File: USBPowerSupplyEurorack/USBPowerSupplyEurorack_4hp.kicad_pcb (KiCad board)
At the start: 2 copper layers, 9.8 x 110 mm, 21 parts, among them J1 1734366-1, J2 95278-501A10LF, Q1 Q_PMOS_GSD

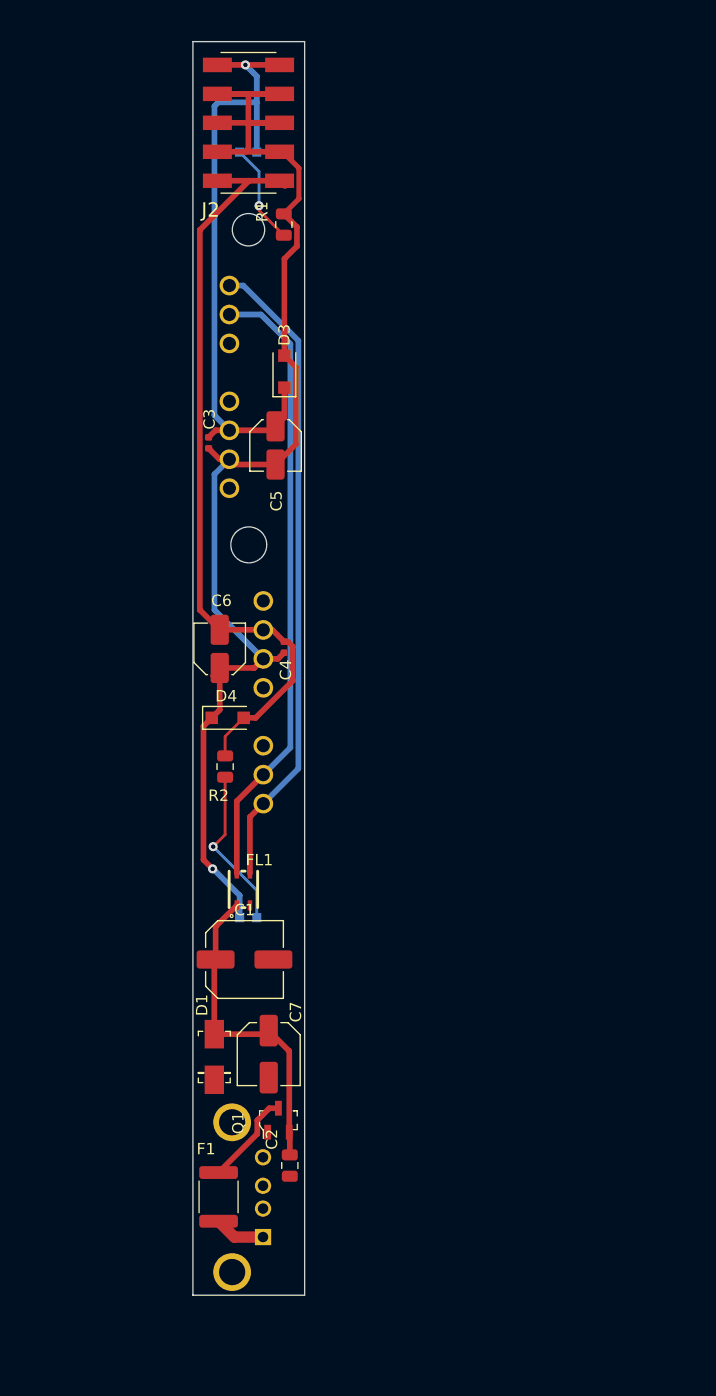
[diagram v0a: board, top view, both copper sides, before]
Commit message: going to 4hp for better routing
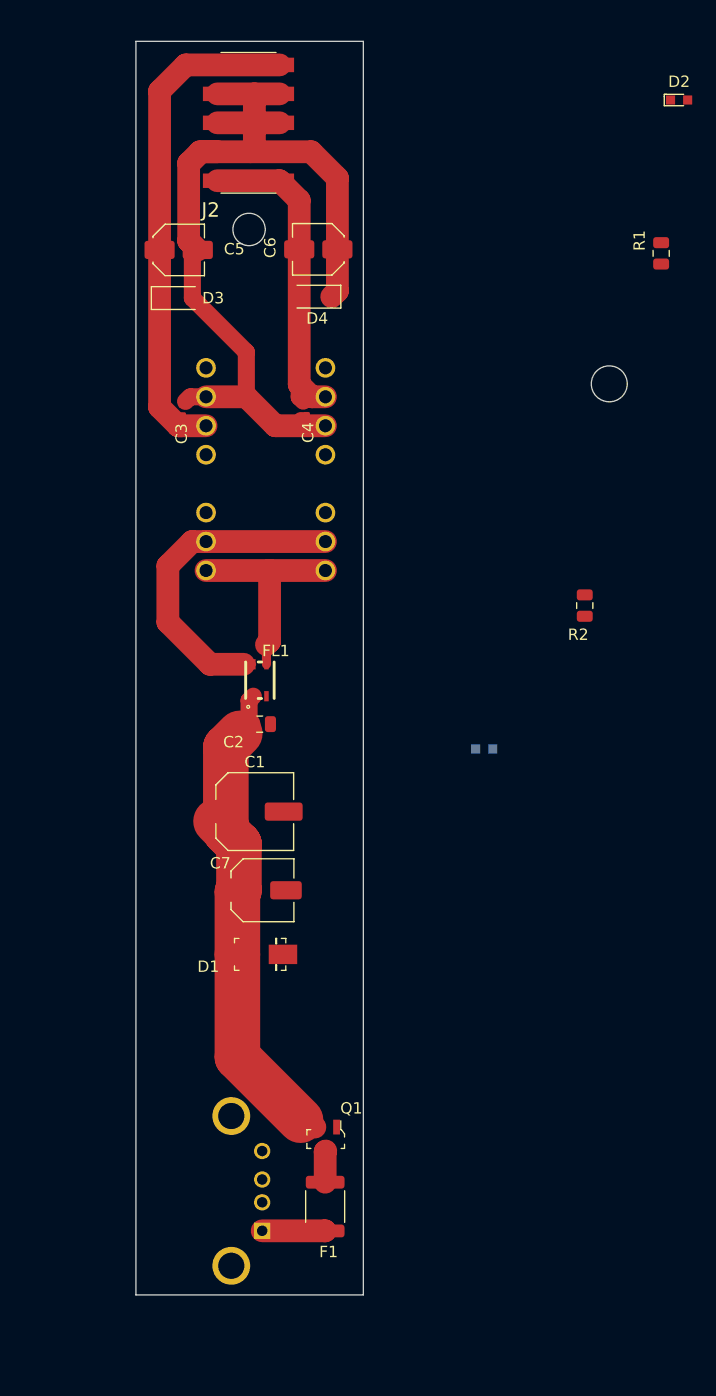
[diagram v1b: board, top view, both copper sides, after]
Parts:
- D2: moved to F.Cu
- F1: value 1812L110 -> 1.1A
- moved C2 38.8 mm to (140.4, 108.0), turned to 0 degrees
- moved D2 38.1 mm to (177.2, 53.2)
- moved D4 37.7 mm to (145.3, 70.5), turned to 180 degrees
- moved C6 36.1 mm to (145.6, 66.3), turned to 180 degrees
- moved R2 34.6 mm to (168.9, 97.6)
- moved R1 33.2 mm to (175.6, 66.7)
- moved D5 25.4 mm to (160.1, 110.2)
- moved PS1 25.1 mm to (135.7, 94.5), turned to 90 degrees
- moved PS2 21.2 mm to (146.2, 94.5)
- moved C4 20.9 mm to (144.5, 80.4)
- moved C5 19.1 mm to (133.3, 66.4), turned to 0 degrees
- moved FL1 18.4 mm to (140.4, 104.2)
- moved C7 14.4 mm to (140.7, 122.6), turned to 0 degrees
- moved C1 13.0 mm to (140.0, 115.7)
- moved D3 11.5 mm to (133.1, 70.6), turned to 0 degrees
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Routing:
- net Net-(C1-Pad1): track 28.7 -> 82.5 mm
- net -12V: track 67.7 -> 28.4 mm
- net +Vin: track 54.8 -> 28.7 mm
- net -Vin: track 56.6 -> 35.6 mm
- net Net-(D5-Pad1): track 14.3 -> 0.00 mm, vias 1 -> 0
- net 0V: track 118.4 -> 106.6 mm, vias 1 -> 0
- net Net-(D2-Pad1): track 8.89 -> 0.00 mm, vias 1 -> 0
- net +5V: track 8.28 -> 2.76 mm
- net Net-(F1-Pad1): track 4.47 -> 5.53 mm
- net +12V: track 56.4 -> 55.7 mm, vias 1 -> 0
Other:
- board size 9.8 x 110 mm -> 43.1 x 110 mm

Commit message: naive placement and routing
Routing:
- net Net-(C1-Pad1): track 82.5 -> 72.7 mm
- net +5V: track 2.76 -> 0.00 mm
- net 0V: track 106.6 -> 107.0 mm, vias 0 -> 9
- added copper zone on F.Cu, net +5V
- added copper zone on F.Cu, net -Vin
- added copper zone on B.Cu, net 0V
- added copper zone on F.Cu, net 0V
- added copper zone on F.Cu, net Net-(C1-Pad1)
- added copper zone on F.Cu, net Net-(F1-Pad1)

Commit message: changed caps on schematics, added PI filter and bigger caps as we have now 4HP
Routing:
- removed copper zone on F.Cu, net +5V
- removed copper zone on F.Cu, net -Vin
- removed copper zone on B.Cu, net 0V
- removed copper zone on F.Cu, net 0V
- removed copper zone on F.Cu, net Net-(C1-Pad1)
- removed copper zone on F.Cu, net Net-(F1-Pad1)
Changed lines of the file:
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@@
   (segment (start 135.7 94.525) (end 141.275 94.525) (width 2) (layer F.Cu) (net 10))
   (segment (start 141.275 94.525) (end 146.175 94.525) (width 2) (layer F.Cu) (net 10))
-  (zone (net 6) (net_name "Net-(F1-Pad1)") (layer F.Cu) (hatch edge 0.508)
-    (connect_pads thru_hole_only (clearance 0.108))
-    (min_thickness 0.254)
-    (fill yes (arc_segments 32) (thermal_gap 0.508) (thermal_bridge_width 0.508) (smoothing fillet) (radius 0.3))
-    (polygon
-      (pts
-        (xy 148.425 154.375) (xy 138.725 154.4) (xy 138.725 150.925) (xy 148.45 150.925)
-      )
-    )
-  )
-  (zone (net 2) (net_name +5V) (layer F.Cu) (hatch edge 0.508)
-    (connect_pads yes (clearance 0.508))
-    (min_thickness 0.254)
-    (fill yes (arc_segments 32) (thermal_gap 0.508) (thermal_bridge_width 0.508) (smoothing fillet) (radius 0.3))
-    (polygon
-      (pts
-        (xy 148.25 145.2) (xy 148.25 149.3) (xy 144.375 149.3) (xy 144.45 146.175) (xy 144.725 145.25)
-        (xy 145.95 144.75) (xy 147.45 144.725)
-      )
-    )
-  )
-  (zone (net 1) (net_name "Net-(C1-Pad1)") (layer F.Cu) (hatch edge 0.508)
-    (connect_pads thru_hole_only (clearance 0.108))
-    (min_thickness 0.254)
-    (fill yes (arc_segments 32) (thermal_gap 0.508) (thermal_bridge_width 0.508) (smoothing fillet) (radius 0.5))
-    (polygon
-      (pts
-        (xy 140.55 105.225) (xy 140.65 108.7) (xy 140.675 108.65) (xy 140.5 109.7) (xy 139.575 111.075)
-        (xy 139.575 116.275) (xy 140.575 117.425) (xy 140.575 121.25) (xy 140.625 136.45) (xy 146.2 141.725)
-        (xy 146.275 142.425) (xy 146.1 143.975) (xy 144.7 144.65) (xy 143.025 144.65) (xy 136.3 137.85)
-        (xy 136.3 121) (xy 134.55 117.1) (xy 134.55 108.725) (xy 136.725 104.775) (xy 140.55 104.775)
-      )
-    )
-  )
-  (zone (net 10) (net_name -Vin) (layer F.Cu) (hatch edge 0.508)
-    (connect_pads thru_hole_only (clearance 0.108))
-    (min_thickness 0.254)
-    (fill yes (arc_segments 32) (thermal_gap 0.508) (thermal_bridge_width 0.508) (smoothing fillet) (radius 0.5))
-    (polygon
-      (pts
-        (xy 146.25 93.65) (xy 146.625 93.675) (xy 146.975 93.95) (xy 147.2 94.3) (xy 147.125 103.225)
-        (xy 141.2 103.225) (xy 140.8 103.25) (xy 140.7 103.025) (xy 140.325 102.0125) (xy 139.725 101.2875)
-        (xy 134.975 95.425) (xy 134.7 94.625) (xy 134.925 93.975) (xy 135.45 93.625)
-      )
-    )
-  )
-  (zone (net 3) (net_name 0V) (layer F.Cu) (hatch edge 0.508)
-    (connect_pads thru_hole_only (clearance 0.254))
-    (min_thickness 0.254)
-    (fill yes (arc_segments 32) (thermal_gap 0.508) (thermal_bridge_width 0.508) (smoothing fillet) (radius 0.5))
-    (polygon
-      (pts
-        (xy 153.35 47.45) (xy 153.725 86.975) (xy 122.125 87.075) (xy 124.125 46.875)
-      )
-    )
-  )
-  (zone (net 3) (net_name 0V) (layer B.Cu) (hatch edge 0.508)
-    (connect_pads thru_hole_only (clearance 0.254))
-    (min_thickness 0.254)
-    (fill yes (arc_segments 32) (thermal_gap 0.508) (thermal_bridge_width 0.508) (smoothing fillet) (radius 0.5))
-    (polygon
-      (pts
-        (xy 154.9 87.15) (xy 121.825 86.925) (xy 119.625 46.475) (xy 157.65 46.475)
-      )
-    )
-  )
 )

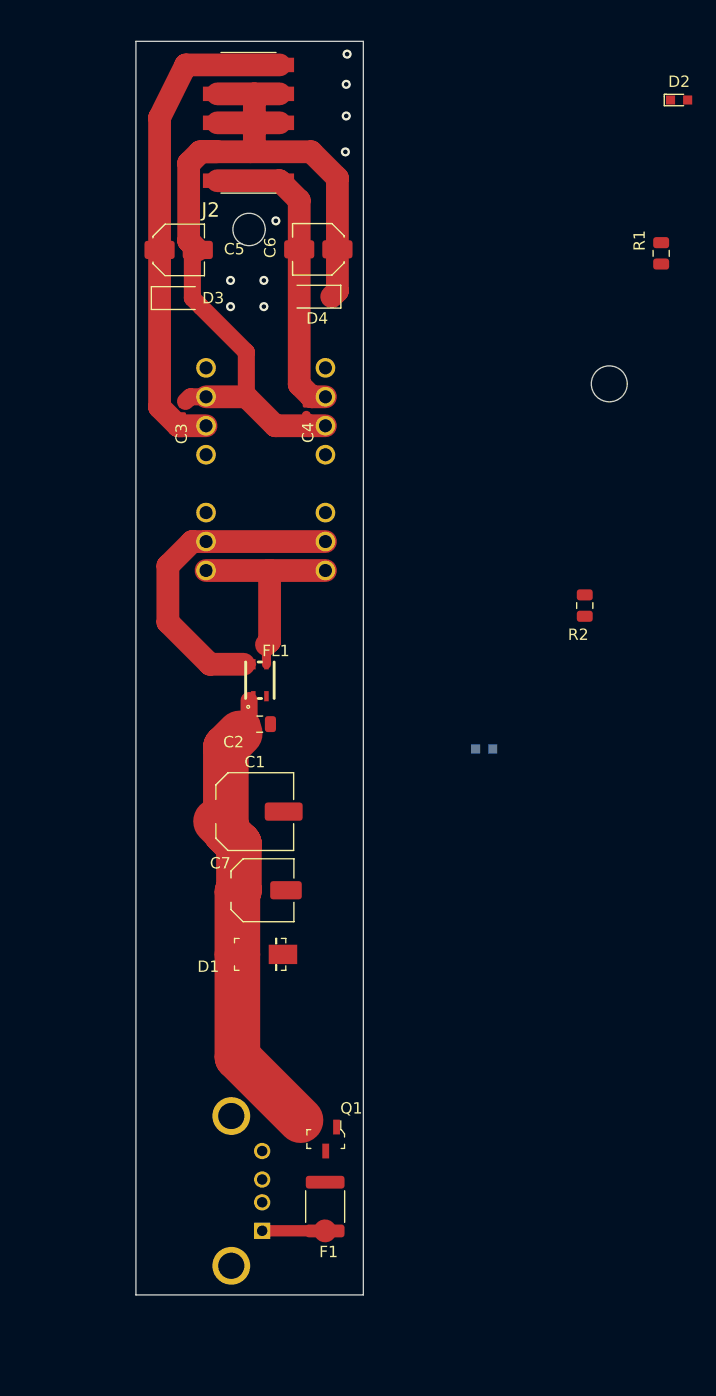
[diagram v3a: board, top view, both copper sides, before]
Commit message: new components placement
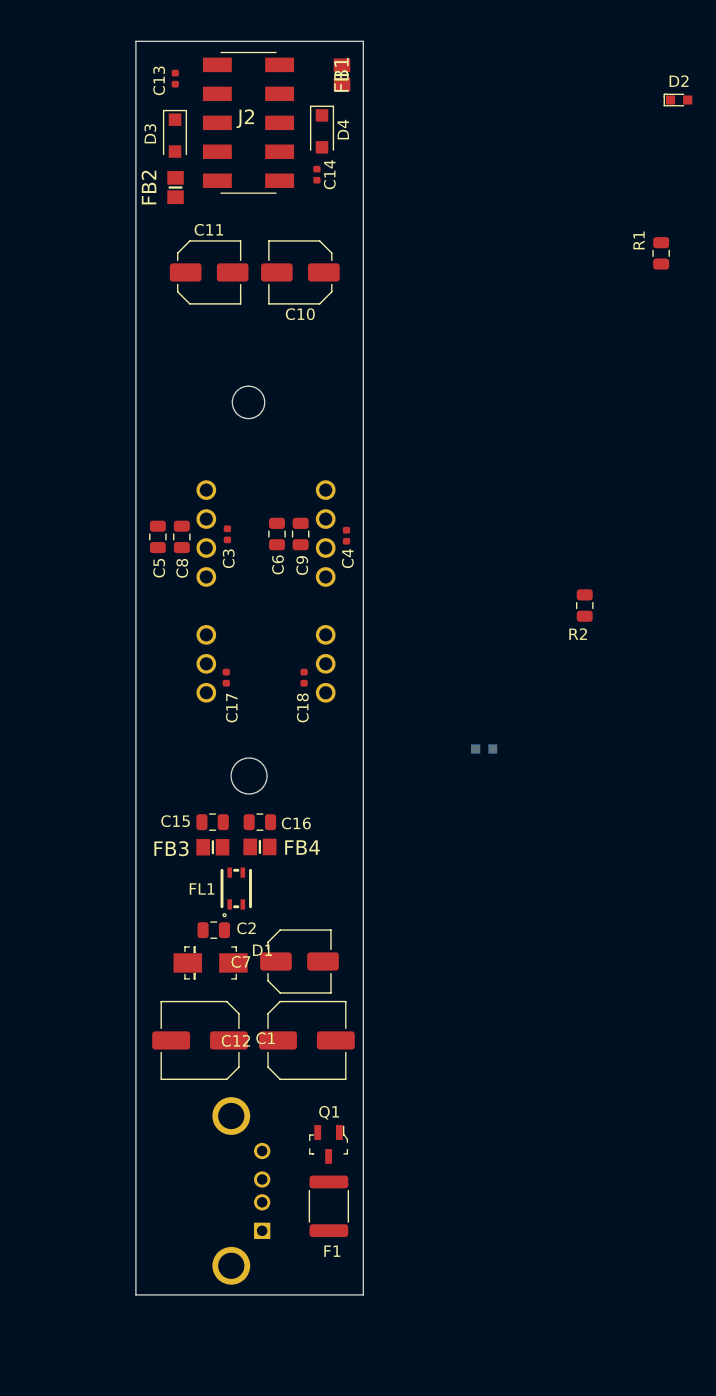
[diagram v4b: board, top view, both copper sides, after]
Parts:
- added C10: 47uF, Capacitor_SMD:C_Elec_5x5.4, F.Cu at (144.0, 68.4)
- added C11: 47uF, Capacitor_SMD:C_Elec_5x5.4, F.Cu at (136.0, 68.4)
- added C12: 220uF, Capacitor_SMD:C_Elec_6.3x7.7, F.Cu at (144.6, 135.8)
- added C13: 100nF, Capacitor_SMD:C_0402_1005Metric, F.Cu at (133.0, 51.4)
- added C14: 100nF, Capacitor_SMD:C_0402_1005Metric, F.Cu at (145.4, 59.8)
- added C15: 22uF, Capacitor_SMD:C_0805_2012Metric, F.Cu at (136.3, 116.6)
- added C16: 22uF, Capacitor_SMD:C_0805_2012Metric, F.Cu at (140.4, 116.6)
- added C17: 100nF, Capacitor_SMD:C_0402_1005Metric, F.Cu at (137.5, 103.9)
- added C18: 100nF, Capacitor_SMD:C_0402_1005Metric, F.Cu at (144.3, 103.9)
- added C8: 22uF, Capacitor_SMD:C_0805_2012Metric, F.Cu at (133.6, 91.6)
- added C9: 22uF, Capacitor_SMD:C_0805_2012Metric, F.Cu at (144.0, 91.3)
- added FB1: C15957, MPZ2012S101AT000:BEADC2012X105N, F.Cu at (147.6, 51.0)
- added FB2: C15957, MPZ2012S101AT000:BEADC2012X105N, F.Cu at (133.0, 60.9)
- added FB3: C15957, MPZ2012S101AT000:BEADC2012X105N, F.Cu at (136.3, 118.8)
- added FB4: C15957, MPZ2012S101AT000:BEADC2012X105N, F.Cu at (140.4, 118.8)
- C5, C6: value 4.7uF -> 22uF; footprint Capacitor_SMD:C_Elec_4x5.4 -> Capacitor_SMD:C_0805_2012Metric
- moved C5 25.2 mm to (131.5, 91.6), turned to 90 degrees
- moved C6 25.2 mm to (141.9, 91.3), turned to 90 degrees
- moved C1 20.6 mm to (135.2, 135.8), turned to 180 degrees
- moved C2 18.5 mm to (136.4, 126.1), turned to 180 degrees
- moved FL1 18.4 mm to (138.3, 122.4)
- moved D4 14.5 mm to (145.9, 56.0), turned to 270 degrees
- moved D3 14.3 mm to (133.0, 56.4), turned to 270 degrees
- moved C4 11.6 mm to (148.0, 91.5)
- moved C3 11.6 mm to (137.6, 91.3)
- moved PS1 10.7 mm to (135.7, 105.2)
- moved PS2 10.7 mm to (146.2, 105.2)
- moved C7 7.04 mm to (143.9, 128.8)
- moved D1 4.41 mm to (136.1, 128.9), turned to 0 degrees
- moved Q1 0.54 mm to (146.4, 144.9)
- moved F1 0.33 mm to (146.5, 150.3)
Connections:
- net -Vin renamed -Vin1
- D3 pad 1: +12V -> Net-(C13-Pad1)
- D3 pad 2: 0V -> Net-(C13-Pad2)
- D4 pad 1: 0V -> Net-(C13-Pad2)
- FL1 pad 4: +Vin -> Net-(FB3-Pad2)
- J2 pad 1: +12V -> Net-(C13-Pad1)
- J2 pad 2: +12V -> Net-(C13-Pad1)
- J2 pad 3: 0V -> Net-(C13-Pad2)
- J2 pad 4: 0V -> Net-(C13-Pad2)
- J2 pad 5: 0V -> Net-(C13-Pad2)
- J2 pad 6: 0V -> Net-(C13-Pad2)
- J2 pad 7: 0V -> Net-(C13-Pad2)
- J2 pad 8: 0V -> Net-(C13-Pad2)
- PS1 pad 2: +Vin -> +Vin1
- PS2 pad 2: +Vin -> +Vin2
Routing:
- net 0V: track 107.0 -> 0.00 mm, vias 9 -> 0
- net Net-(C1-Pad1): track 72.7 -> 0.00 mm
- net +12V: track 55.3 -> 0.00 mm
- net -Vin1: track 35.6 -> 0.00 mm
- net -12V: track 28.8 -> 0.00 mm
- net +Vin: track 28.7 -> 0.00 mm
- net Net-(F1-Pad1): track 5.53 -> 0.00 mm
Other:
- board size 43.1 x 110 mm -> 19.9 x 110 mm

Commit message: still testing routing
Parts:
- moved C7 0.15 mm to (143.9, 129.0)
- moved C16 0.05 mm to (140.4, 116.6)
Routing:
- net -12V: track 0.00 -> 52.7 mm
- net 0V: track 0.00 -> 41.9 mm
- net Net-(C13-Pad2): track 0.00 -> 39.2 mm
- net Net-(C1-Pad1): track 0.00 -> 31.6 mm
- net -Vin1: track 0.00 -> 26.1 mm
- net +12V: track 0.00 -> 23.5 mm
- net +Vin2: track 0.00 -> 21.5 mm
- net +Vin1: track 0.00 -> 17.3 mm
- net Net-(C13-Pad1): track 0.00 -> 14.9 mm
- net Net-(F1-Pad1): track 0.00 -> 5.86 mm
- net Net-(FB3-Pad2): track 0.00 -> 4.92 mm
- net +5V: track 0.00 -> 2.25 mm
- added copper zone on F.Cu, net GND

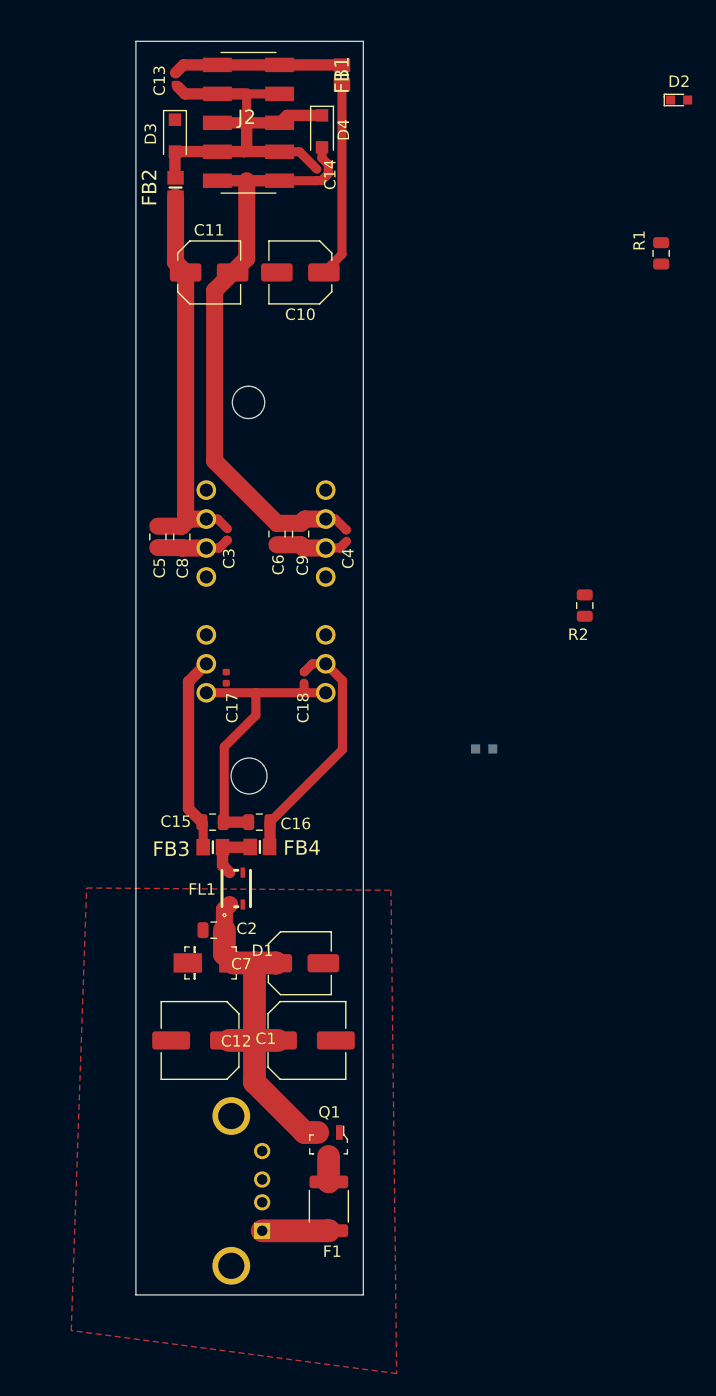
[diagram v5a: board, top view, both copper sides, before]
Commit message: changing placement of components
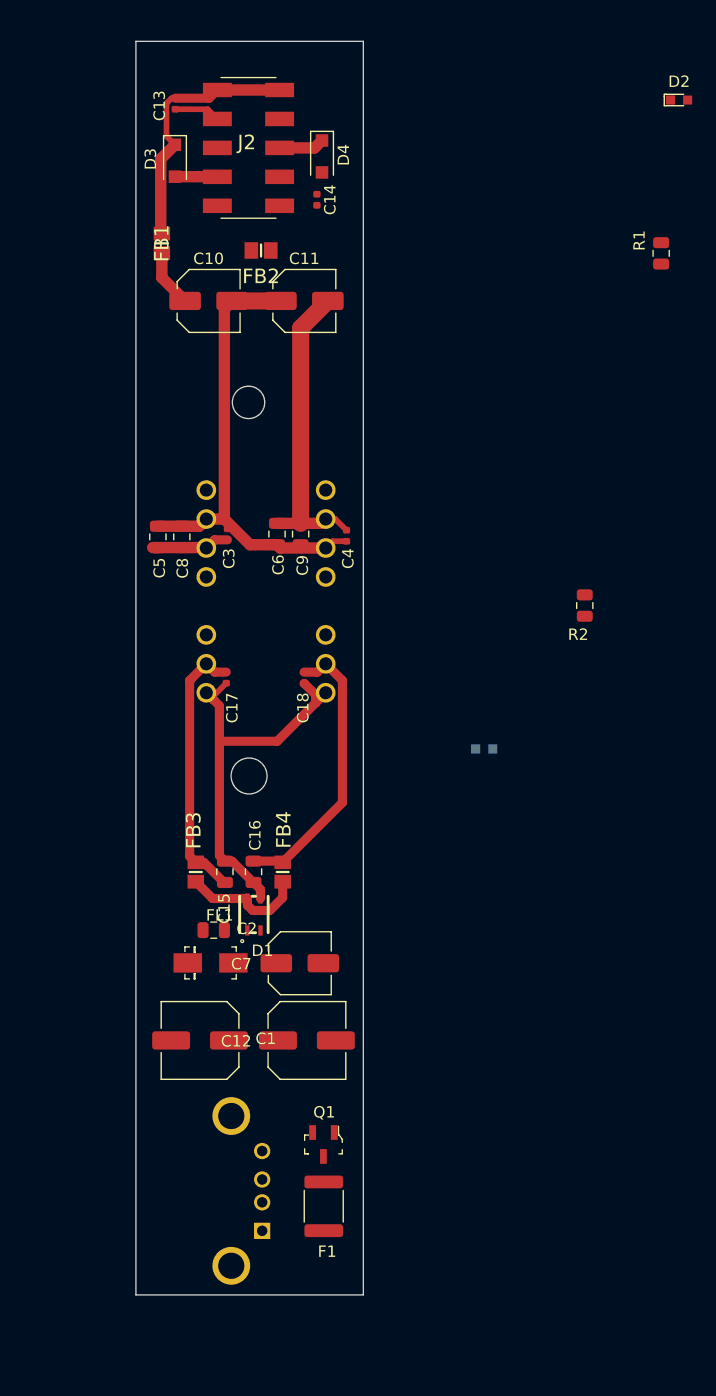
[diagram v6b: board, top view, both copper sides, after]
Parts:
- moved FB1 21.6 mm to (131.8, 65.8)
- moved FB2 9.32 mm to (140.5, 66.5), turned to 0 degrees
- moved C11 8.72 mm to (144.3, 70.9)
- moved C10 8.43 mm to (135.9, 70.9), turned to 0 degrees
- moved C15 4.49 mm to (137.4, 121.0), turned to 90 degrees
- moved C16 4.38 mm to (139.9, 121.0), turned to 270 degrees
- moved FB4 2.97 mm to (142.4, 121.0), turned to 270 degrees
- moved FL1 2.75 mm to (139.9, 124.7)
- moved FB3 2.64 mm to (134.8, 121.0), turned to 270 degrees
- moved C13 2.20 mm to (133.0, 53.6)
- moved C14 2.20 mm to (145.4, 62.0)
- moved D3 2.20 mm to (133.0, 58.6)
- moved D4 2.20 mm to (145.9, 58.2)
- moved J2 2.20 mm to (139.4, 57.5)
- moved F1 0.45 mm to (146.0, 150.3)
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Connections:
- C13 pad 2: Net-(C13-Pad2) -> 0V
- C14 pad 1: Net-(C13-Pad2) -> 0V
- C14 pad 2: -12V -> Net-(C14-Pad2)
- D3 pad 2: Net-(C13-Pad2) -> 0V
- D4 pad 1: Net-(C13-Pad2) -> 0V
- D4 pad 2: -12V -> Net-(C14-Pad2)
- FB2 pad 1: Net-(C13-Pad2) -> Net-(C14-Pad2)
- FB2 pad 2: 0V -> -12V
- J2 pad 10: -12V -> Net-(C14-Pad2)
- J2 pad 3: Net-(C13-Pad2) -> 0V
- J2 pad 4: Net-(C13-Pad2) -> 0V
- J2 pad 5: Net-(C13-Pad2) -> 0V
- J2 pad 6: Net-(C13-Pad2) -> 0V
- J2 pad 7: Net-(C13-Pad2) -> 0V
- J2 pad 8: Net-(C13-Pad2) -> 0V
- J2 pad 9: -12V -> Net-(C14-Pad2)
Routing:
- net Net-(C13-Pad2): track 39.2 -> 0.00 mm
- net Net-(C1-Pad1): track 31.6 -> 0.00 mm
- net -12V: track 52.7 -> 27.2 mm
- net 0V: track 41.9 -> 53.6 mm
- net +12V: track 23.5 -> 12.2 mm
- net -Vin1: track 26.1 -> 35.6 mm
- net Net-(C13-Pad1): track 14.9 -> 22.7 mm
- net +Vin1: track 17.3 -> 23.6 mm
- net Net-(FB3-Pad2): track 4.92 -> 10.9 mm
- net Net-(F1-Pad1): track 5.86 -> 0.00 mm
- net +Vin2: track 21.5 -> 25.0 mm
- net +5V: track 2.25 -> 0.00 mm
- removed copper zone on F.Cu, net GND
